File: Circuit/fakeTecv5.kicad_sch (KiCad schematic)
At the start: 74 parts, among them J1 EXTRA, J11 FET1 3,3, J12 FET2 3,3, J13 FET3 3,3, J14 GPS Pins, J16 Encoder Pads, J37 SCL, J38 QWIIC, J39 SDA, J40 3.3V, J41 GND, J42 FET1, J43 FET2, J44 FET3, J45 GND, J46 3.3V, J47 GND, J48 GND, J49 GND, J5 I2C Oled screen, J6 FET1 Drain, J7 FET2 Drain, J8 FET3 Drain, J9 Battery Connector, Q1 AO3400A, Q2 AO3400A, Q3 AO3400A, SW1 Reset, SW2 SW_Push, U1 XB8089D0, U2 HT-RA62, U3 nice!nano v2

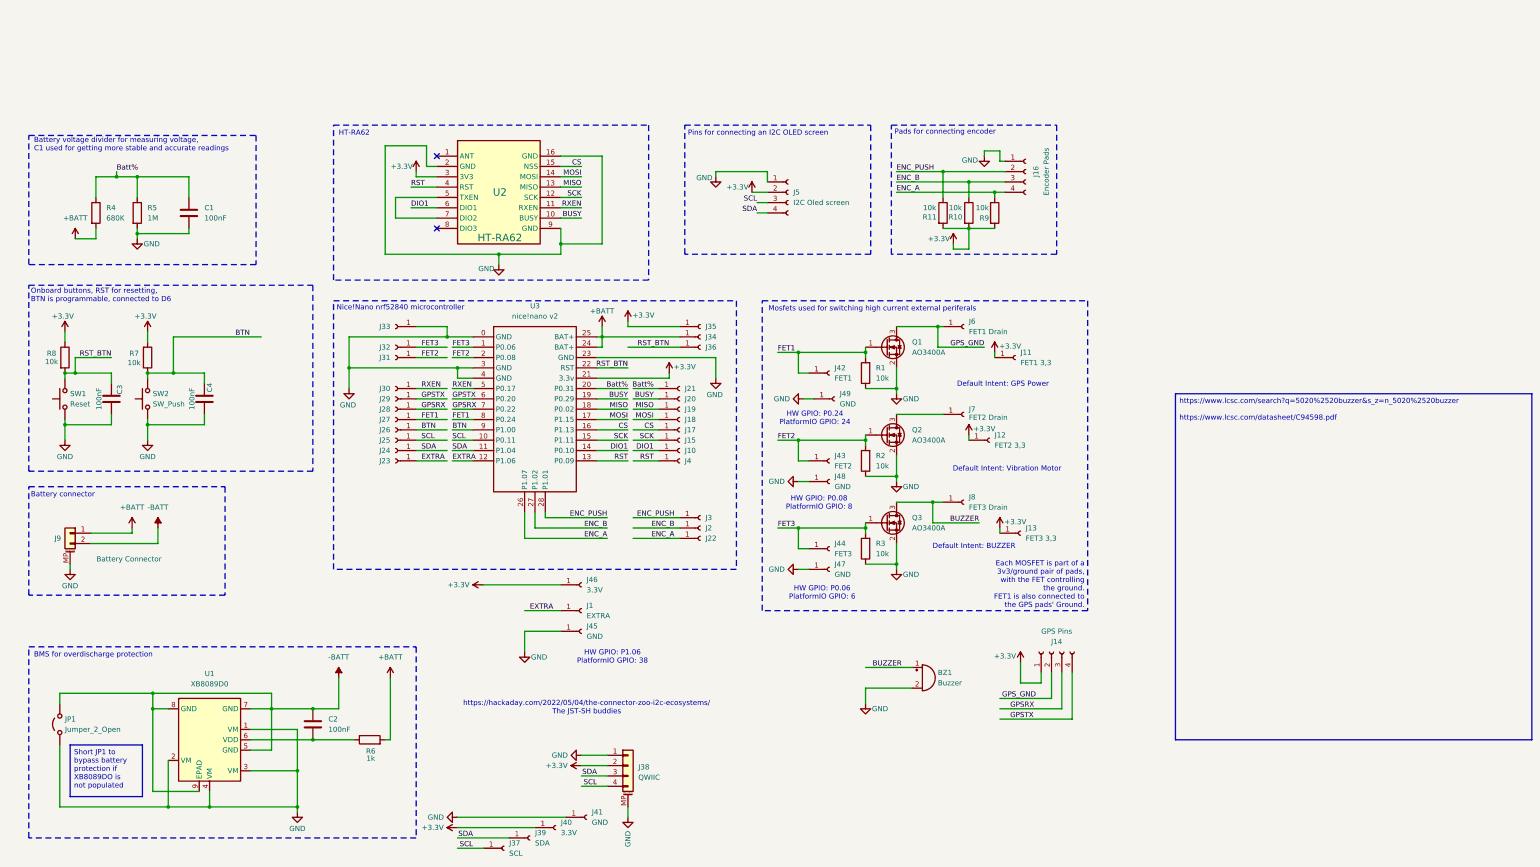
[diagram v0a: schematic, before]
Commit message: schematic layout update
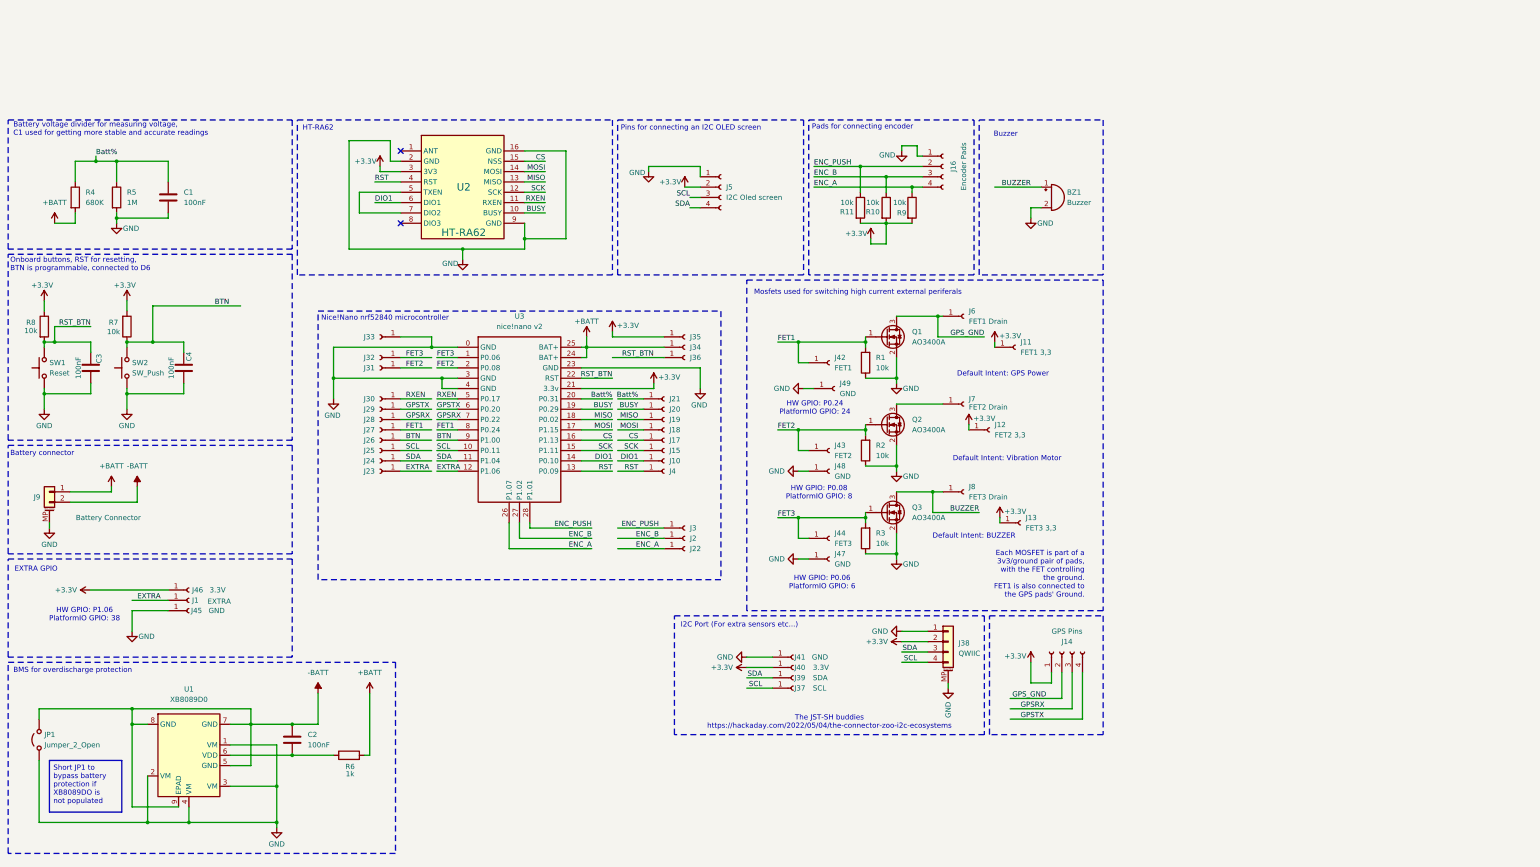
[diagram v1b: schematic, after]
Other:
- note added: "Buzzer"
- note added: "EXTRA GPIO"
- note added: "I2C Port (For extra sensors etc...)"
- note added: "The JST-SH buddies https://hackaday.com/2022/05/04/the-connector-zoo-i2c-ecosystems"
- note removed: "https://hackaday.com/2022/05/04/the-connector-zoo-i2c-ecosystems/ The JST-SH buddies"
- moved on the sheet: BZ1, C1, C2, C3, C4, J1, J10, J11, J12, J13, J14, J15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

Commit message: Rename from rotTec_pcb to roTec and pdf and clean up schematic and pcb
Also add 3D printed case with fixed usb Type-C port position
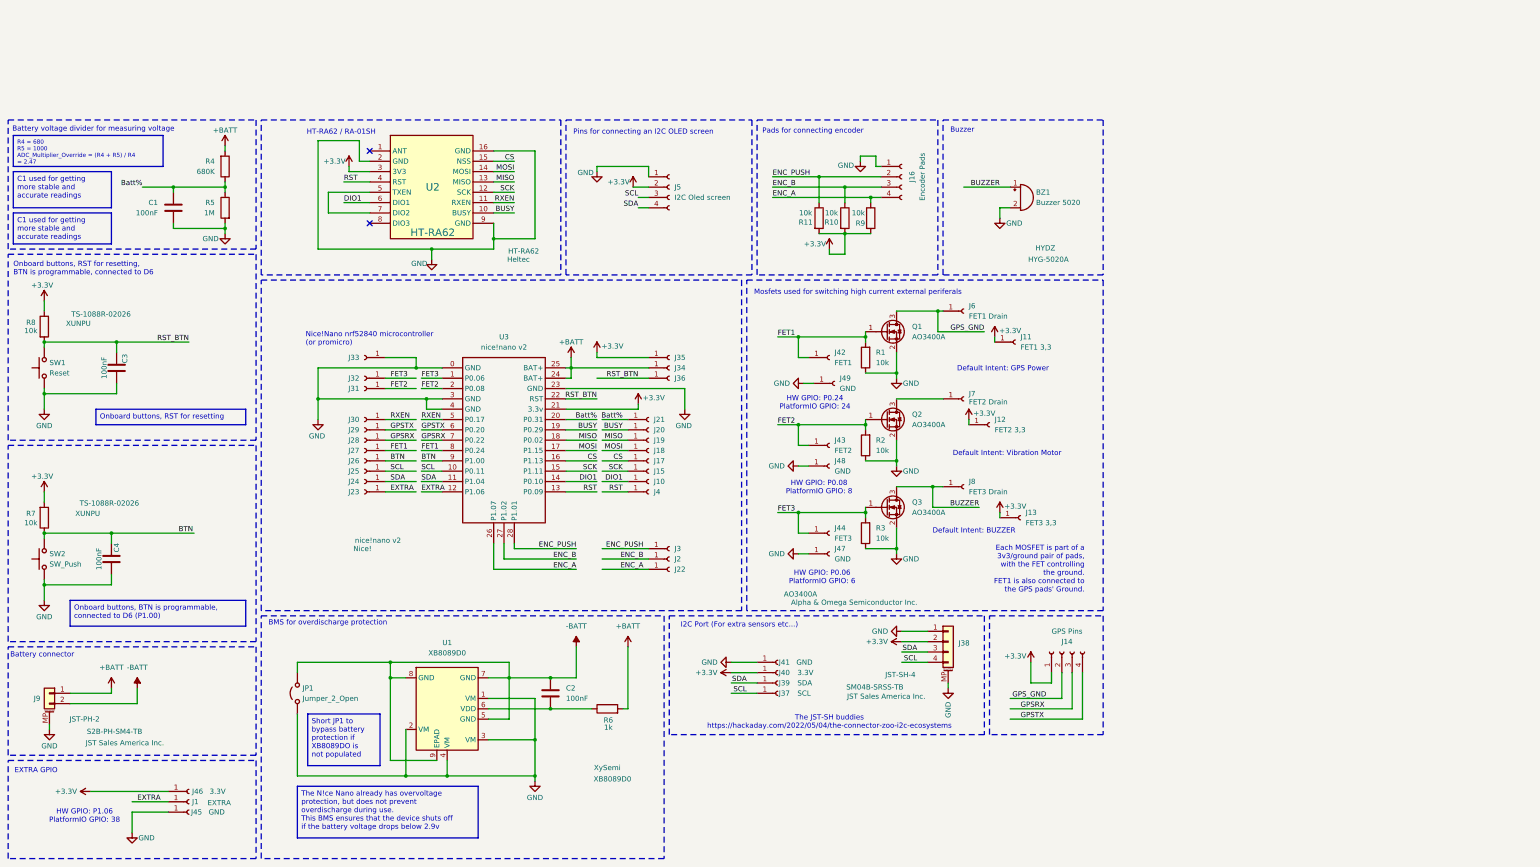
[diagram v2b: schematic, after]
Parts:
- BZ1: value Buzzer -> Buzzer 5020; MPD (none) -> 75dB 4kHz 3V SMD,5x5mm Alarms, Buzzers, and Sirens RoHS; MPL (none) -> https://www.lcsc.com/product-detail/C7544810.html?s_z=n_buz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; MPN (none) -> HYG-5020A; Manufacturer (none) -> HYDZ; Package (none) -> SMD,5x5mm; Shopping (none) -> https://www.lcsc.com/search?q=Buzzer_5020&s_z=n_Buzzer_5020
- C1, C2, C3, C4: Package (none) -> 0805; Shopping (none) -> https://www.lcsc.com/search?q=100nF%25200805&s_z=n_100nF%25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
- J11, J12, J13, J14, J16, J23, J37, J39, J40, J41, J42, J43, J44, J46, J47, J48, J49, J6, J7, J8, JP1: now left out of the parts list
- J38: value QWIIC -> JST-SH-4; MPD (none) -> 4P 1x4P Tin 1mm 50V 4 1A 1 Surface Mount, Right Angle -25℃~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; MPL (none) -> https://www.lcsc.com/product-detail/C51940130.html?s_z=n_SM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; MPN (none) -> SM04B-SRSS-TB; Manufacturer (none) -> JST Sales America Inc.; Package (none) -> SMD,P=1mm,Surface Mount,Right Angle; Shopping (none) -> https://www.lcsc.com/search?q=SM04B-SRSS-TB&s_z=n_SM04B-SRS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
- J5: MPD (none) -> 1x4P 4P Gold Brass -40℃~+105℃ Black Pin Header 2.54mm 2.5mm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; MPL (none) -> https://www.lcsc.com/product-detail/C32713270.html?s_z=n_1%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; MPN (none) -> HX PZ2.54-1x4P ZZ; Manufacturer (none) -> Hanxia; Package (none) -> Through Hole,P=2.54mm; Shopping (none) -> https://www.lcsc.com/search?q=1%2a4P%25202.54mm%2520header&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
- J9: value Battery Connector -> JST-PH-2; MPD (none) -> 2P 1x2P PH Tin -25℃~+85℃ Beige 2mm 100V 2 2A 1 Surface Moun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; MPL (none) -> https://www.lcsc.com/product-detail/C295747.html?s_z=n_S2B-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; MPN (none) -> S2B-PH-SM4-TB; Manufacturer (none) -> JST Sales America Inc.; Package (none) -> SMD,P=2mm,Surface Mount,Right Angle; Shopping (none) -> https://www.lcsc.com/search?q=S2B-PH-SM4-TB&s_z=n_S2B-PH-SM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
- Q1, Q2, Q3: MPD (none) -> 30V 5.7A 48mΩ@2.5V 1.4W SOT-23-3L Single FETs, MOSFETs RoHS; MPL (none) -> https://www.lcsc.com/product-detail/C20917.html?s_z=n_AO340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; MPN (none) -> AO3400A; Manufacturer (none) -> Alpha & Omega Semiconductor Inc.; Package (none) -> SOT-23-3L; Shopping (none) -> https://www.lcsc.com/search?q=MOSFET%2520N-CH%2520SOT-23-3L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
- R1, R10, R11, R2, R3, R7, R8, R9: Package (none) -> 0805; Shopping (none) -> https://www.lcsc.com/search?q=10K%25200805&s_z=n_10K%252008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
- R4: Package (none) -> 0805; Shopping (none) -> https://www.lcsc.com/search?q=680K%25200805&s_z=n_680K%2520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
- R5: Package (none) -> 0805; Shopping (none) -> https://www.lcsc.com/search?q=1M%25200805&s_z=n_1M%25200805
- R6: Package (none) -> 0805; Shopping (none) -> https://www.lcsc.com/search?q=1k%25200805&s_z=n_1k%25200805
- SW1, SW2: footprint Button_Switch_SMD:SW_Push_SPST_NO_Alps_SKRK -> faketec:SW_Push_SPST_NO_Alps_SKRK; MPD (none) -> Without Bracket 3.9mm 12V 2.93mm Round Button SPST 50mA SMD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; MPL (none) -> https://www.lcsc.com/product-detail/C455280.html?s_z=n_TS-1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; MPN (none) -> TS-1088R-02026; Manufacturer (none) -> XUNPU; Package (none) -> SMD,4x3mm; Shopping (none) -> https://www.lcsc.com/search?q=TS-1088R-02026&s_z=n_TS-1088R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
- U1: MPD (none) -> One Cell Lithium-ion/Polymer Battery Protection IC; MPL (none) -> https://www.lcsc.com/product-detail/C2760005.html; MPN (none) -> XB8089D0; Manufacturer (none) -> XySemi; Package (none) -> SOIC-8; Shopping (none) -> https://www.lcsc.com/search?q=XB8089D0&s_z=n_XB8089D0
- U2: ALTIUM_VALUE HT-RA62 -> (none); MPD (none) -> HT-RA62 Module SX1262 Secondary Development Supports LoRaWA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; MPL (none) -> https://www.aliexpress.com/item/1005005543917617.html; MPN (none) -> HT-RA62; Manufacturer (none) -> Heltec; Package (none) -> HT-RA62; Shopping (none) -> https://www.aliexpress.com/w/wholesale-HT%252525252dRA62-1%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
- U3: MPD (none) -> Pro NRF52840 Development Board Compatible with Nice!Nano V2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; MPL (none) -> https://www.aliexpress.com/item/1005010222966695.html; MPN (none) -> nice!nano v2; Manufacturer nice! -> Nice!; Package (none) -> nice!nano v2; Shopping (none) -> https://www.aliexpress.com/w/wholesale-NRF52840-1%2525252d1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
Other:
- note added: "Battery voltage divider for measuring voltage"
- note added: "HT-RA62 / RA-01SH"
- note added: "Nice!Nano nrf52840 microcontroller (or promicro)"
- note removed: "Battery voltage divider for measuring voltage, C1 used for getting more stable and accurate readings"
- note removed: "HT-RA62"
- note removed: "Nice!Nano nrf52840 microcontroller"
- title: fakeTec v5 -> roTec v5 (faketec v5 fork)
- moved on the sheet: BZ1, C1, C2, C3, C4, J1, J10, J11, J12, J13, J15, J16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

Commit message: update bom
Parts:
- U1: MPL https://www.lcsc.com/product-detail/C2760005.html -> https://www.lcsc.com/product-detail/C2760005.html?s_z=n_XyS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
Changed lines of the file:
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@@
 			)
 		)
-		(property "MPL" "https://www.lcsc.com/product-detail/C2760005.html"
+		(property "MPL" "https://www.lcsc.com/product-detail/C2760005.html?s_z=n_XySemi%2520XB8089D0"
 			(at 121.92 158.75 0)
 			(effects

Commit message: bom shopping link typo
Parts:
- U2: Shopping https://www.aliexpress.com/w/wholesale-HT%252525252dRA62-1%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 -> https://www.aliexpress.com/w/wholesale-HT%2525252dRA62.html
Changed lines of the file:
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@@
 			)
 		)
-		(property "Shopping" "https://www.aliexpress.com/w/wholesale-HT%252525252dRA62-1%252525252d10pc.html"
+		(property "Shopping" "https://www.aliexpress.com/w/wholesale-HT%2525252dRA62.html"
 			(at 118.11 30.48 0)
 			(effects

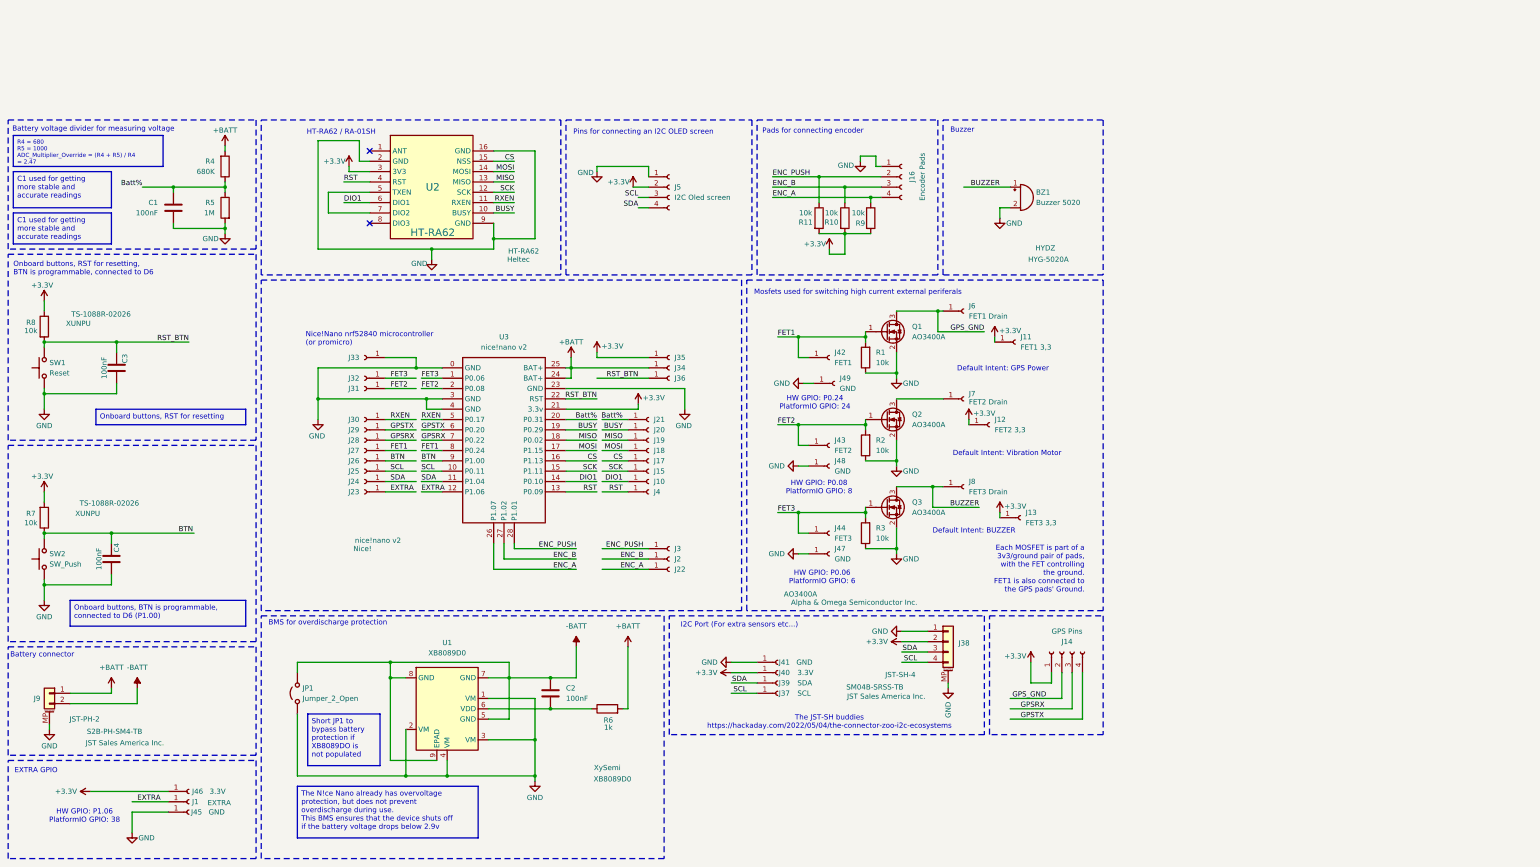
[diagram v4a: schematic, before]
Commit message: clean up schematic and resolve all schematic design rule checks
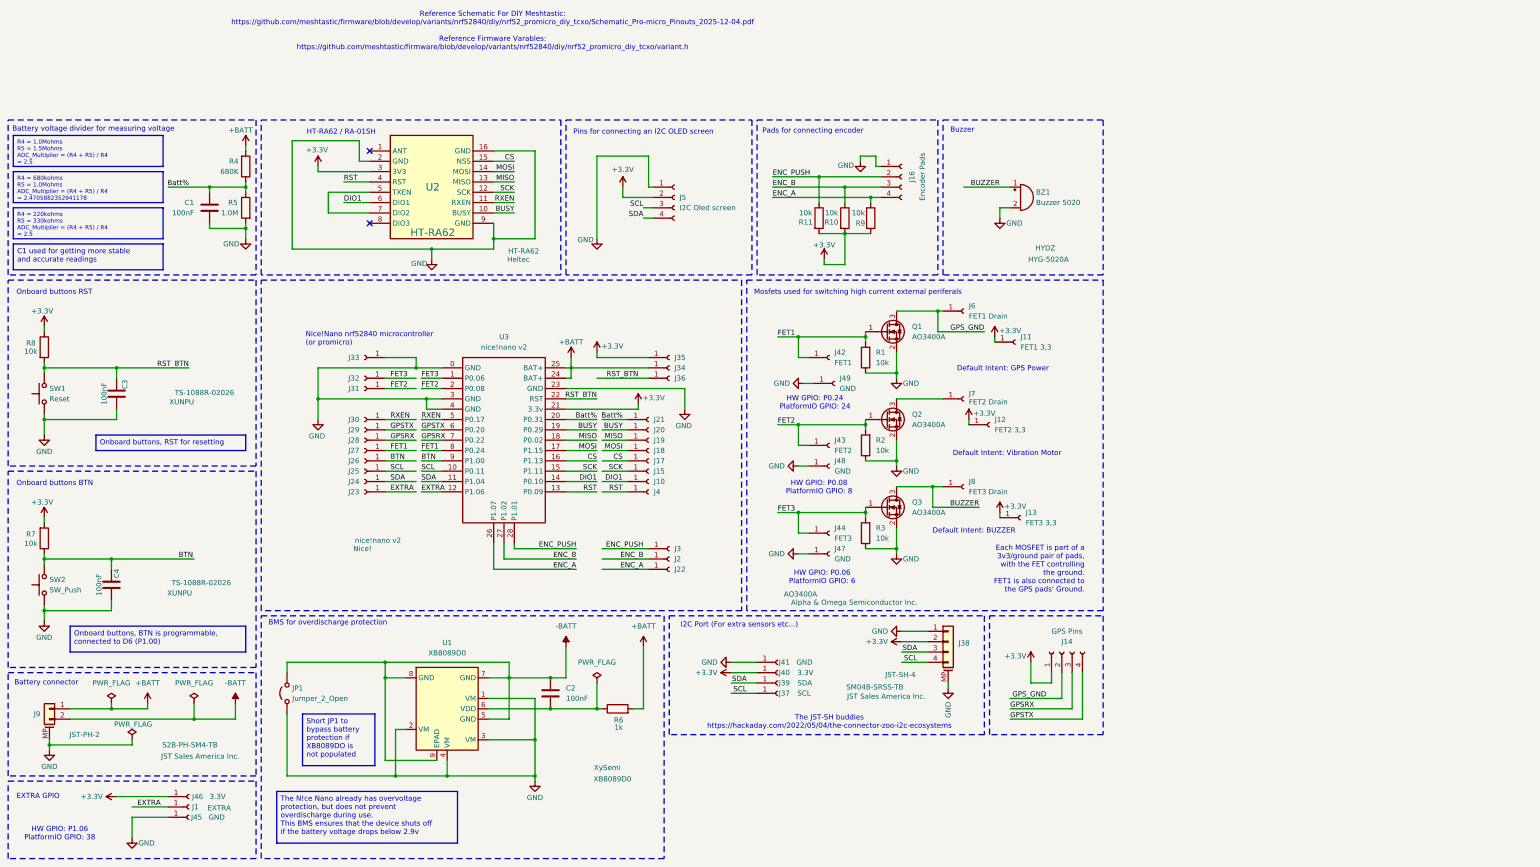
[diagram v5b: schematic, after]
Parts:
- R5: value 1M -> 1.0M
- U1: symbol Regulator_Switching:LM25085MY -> faketec:LM25085MY
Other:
- note added: "Onboard buttons BTN"
- note added: "Onboard buttons RST"
- note added: "Reference Schematic For DIY Meshtastic: https://github.com/meshtastic/firmware/blob/develop/variants/nrf52840/diy/nrf52_promicro_diy_tcxo/Schematic_Pro-micro_Pinouts_2025-12-04.pdf Reference Firmware Varables: https://github.com/meshtastic/firmware/blob/develop/variants/nrf52840/diy/nrf52_promicro_diy_tcxo/variant.h"
- note removed: "Onboard buttons, RST for resetting, BTN is programmable, connected to D6"
- moved on the sheet: C1, C3, C4, J1, J45, J46, J5, J9, JP1, R4, R5, R6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

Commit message: Removed resistor and capacitor for button and also add integrated test pads.
Also added jlcpcb design rules
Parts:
- removed C3, C4: 100nF, Capacitor_SMD:C_0805_2012Metric_Pad1.18x1.45mm_HandSolder, symbol Device:C
- removed R7, R8: 10k, Resistor_SMD:R_0805_2012Metric_Pad1.20x1.40mm_HandSolder, symbol Device:R
